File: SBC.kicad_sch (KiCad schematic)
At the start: 0 parts

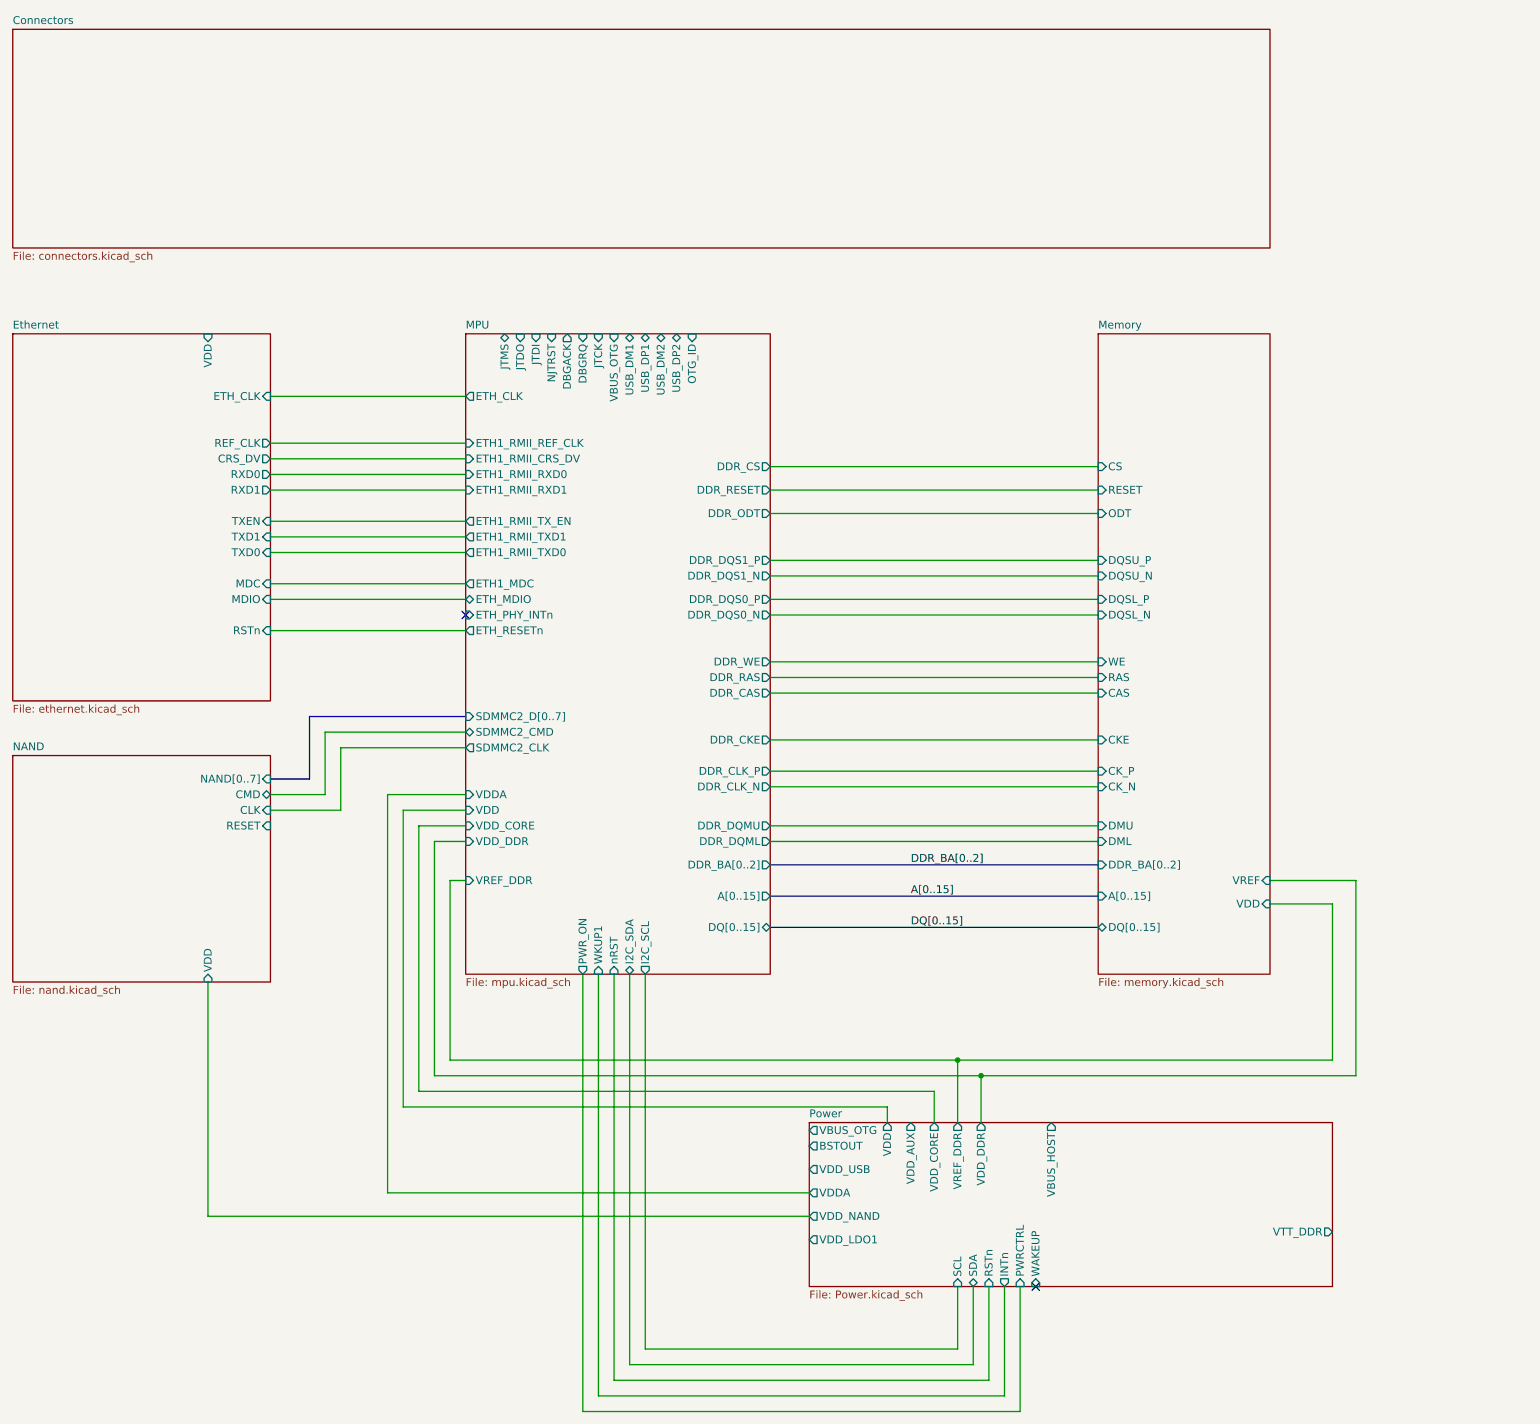
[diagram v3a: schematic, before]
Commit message: Moved connectors to their own sheets
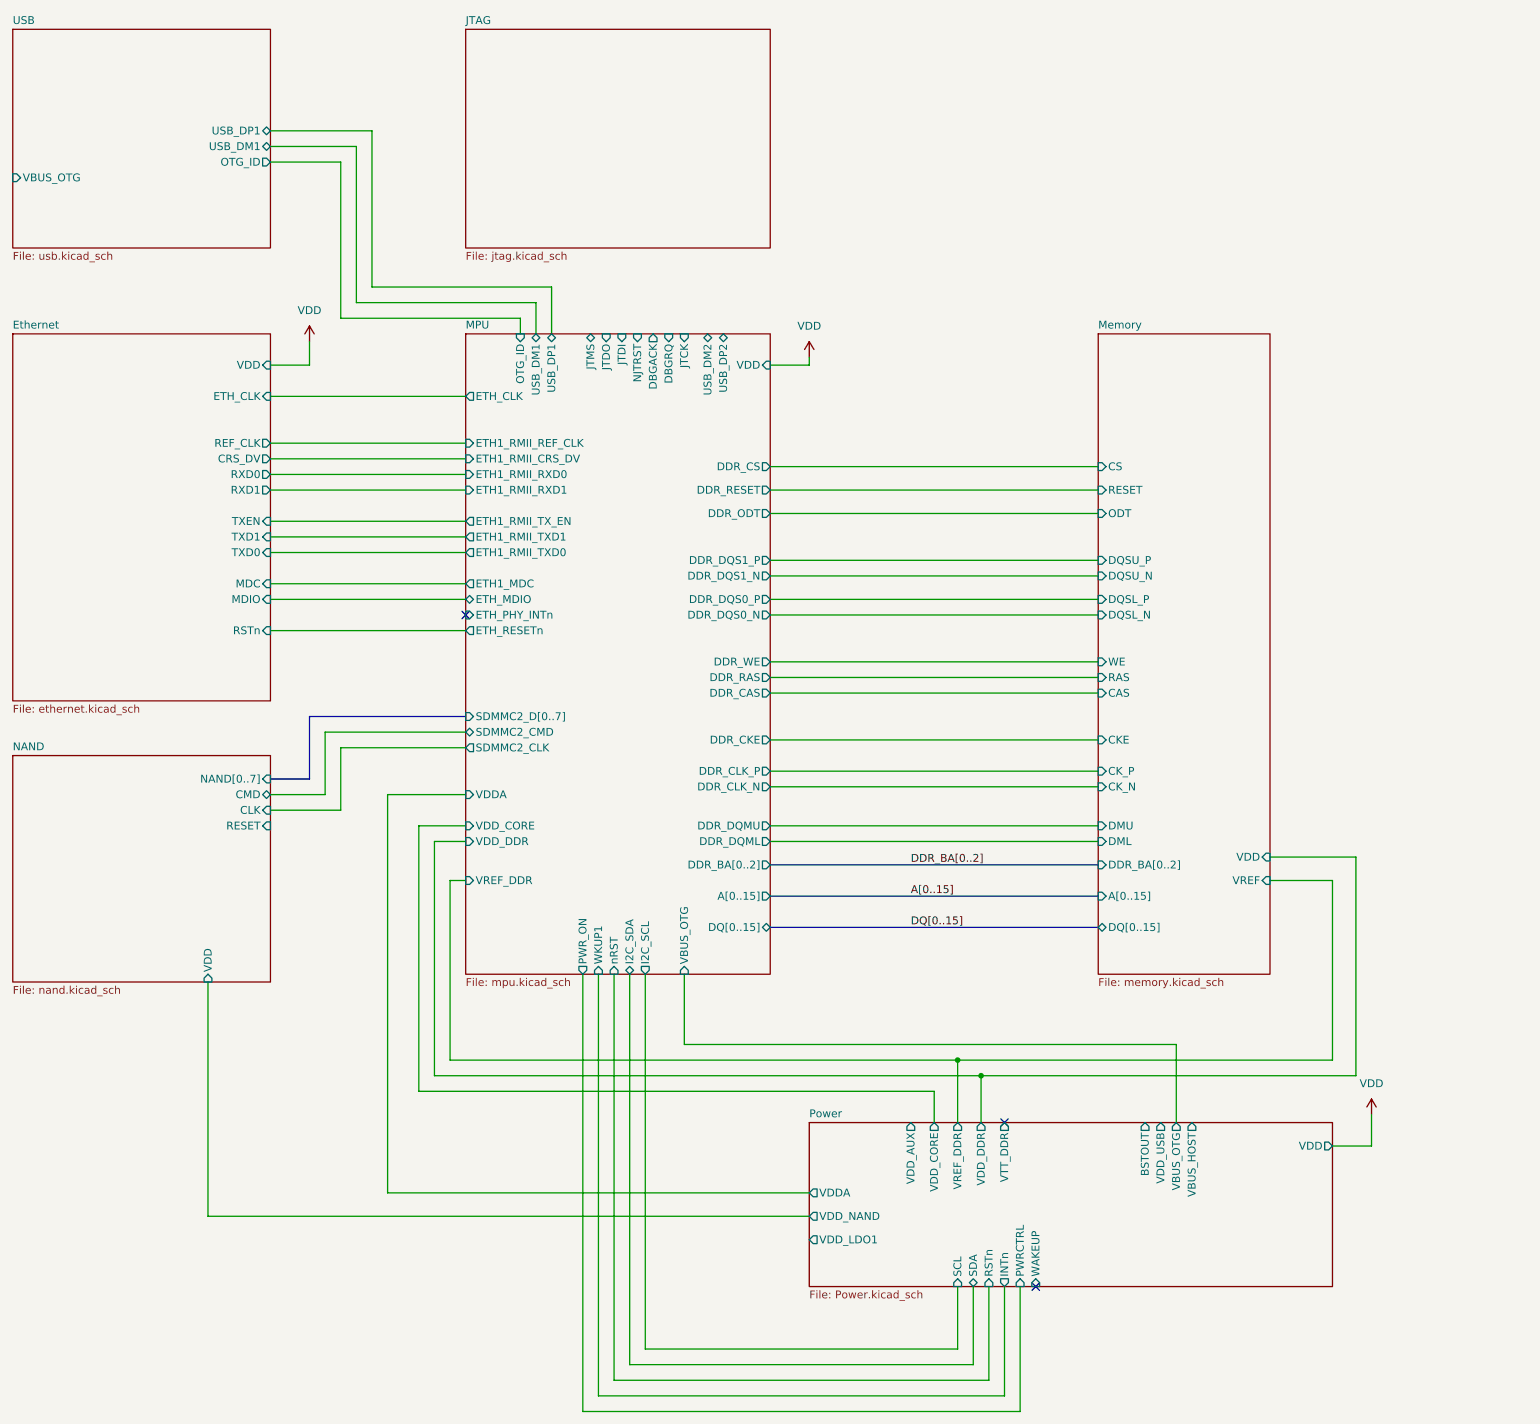
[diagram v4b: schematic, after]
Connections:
- no-connect marks 2 -> 3
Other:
- sheet Connectors renamed JTAG
- added sheet USB (usb.kicad_sch)
- sheet JTAG: file connectors.kicad_sch -> jtag.kicad_sch

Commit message: Finished USB JTAG connectors and cleaned up schematic
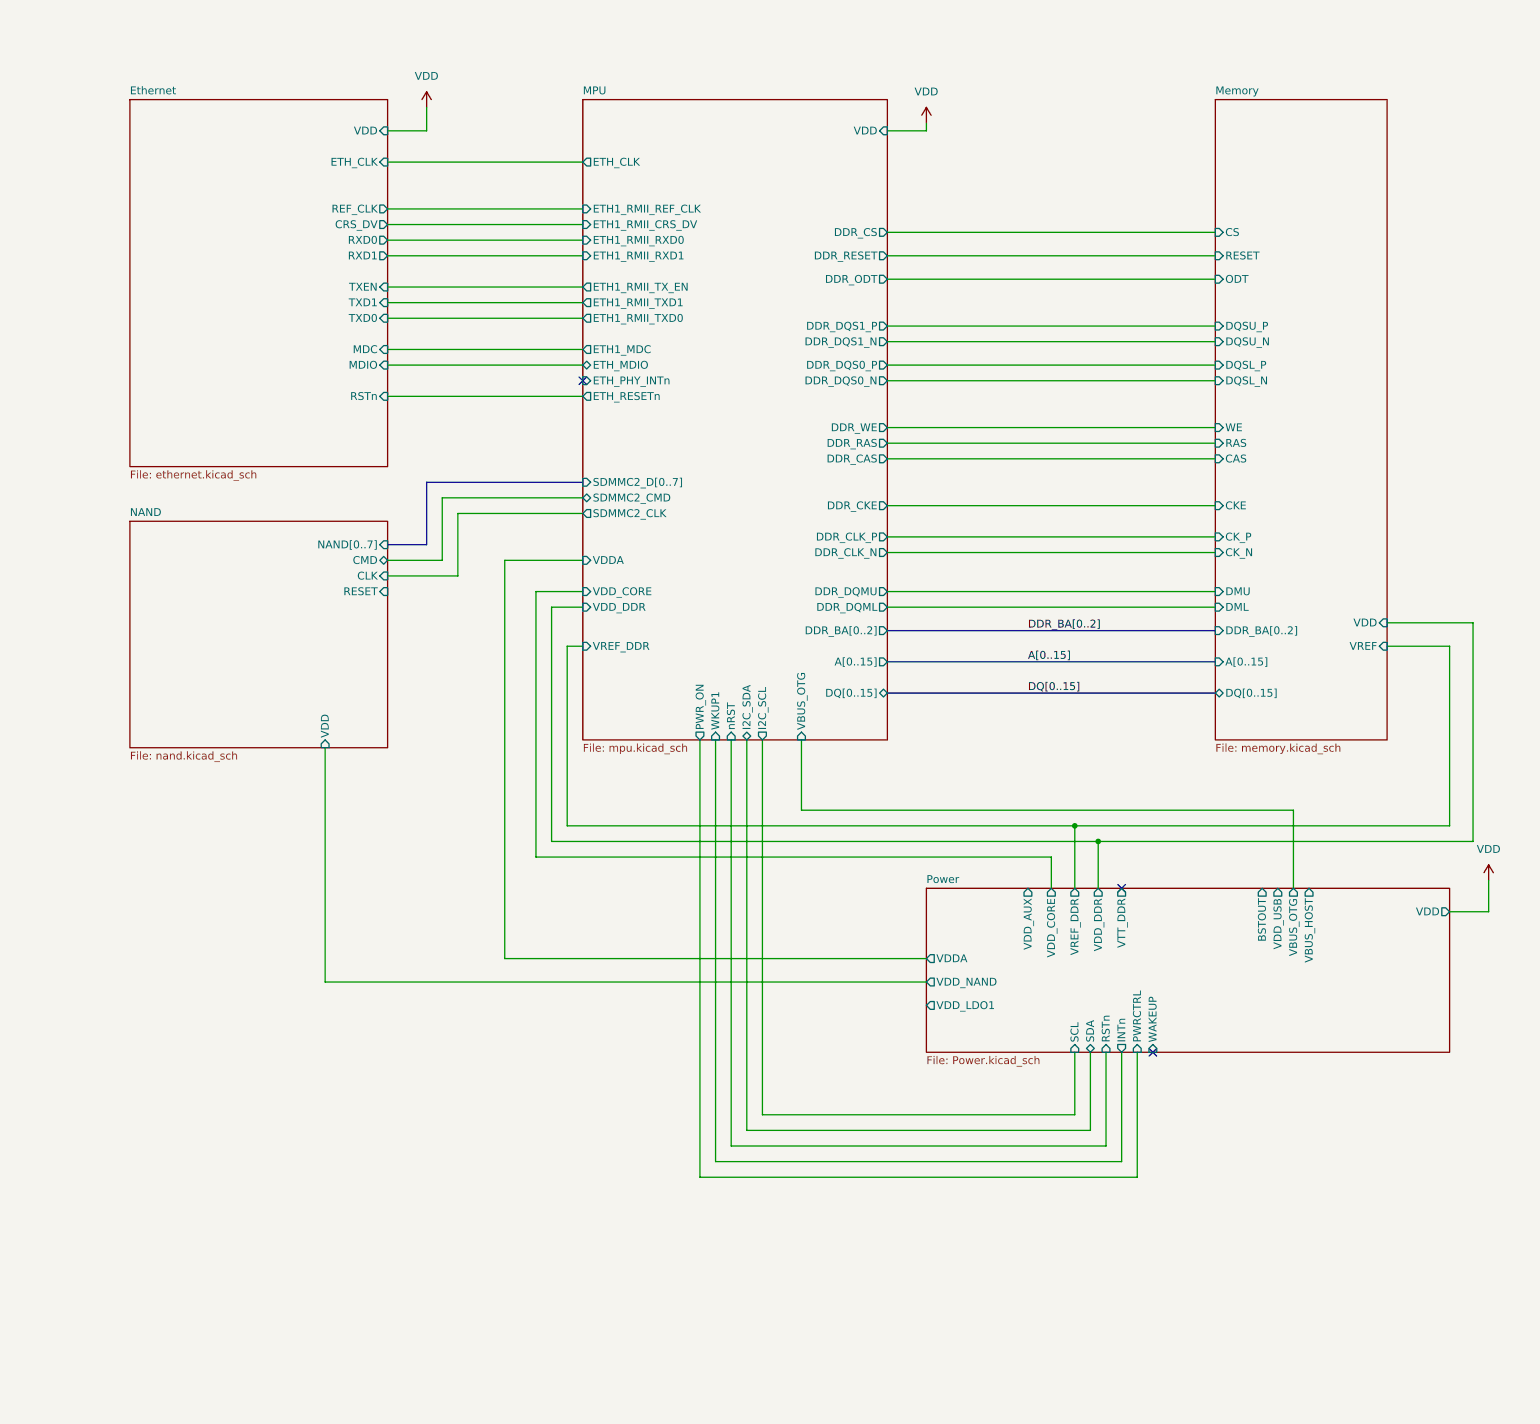
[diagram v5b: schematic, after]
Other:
- removed sheet JTAG
- removed sheet USB
- sheet MPU ports: added none; removed DBGACK, DBGRQ, JTCK, JTDI, JTDO, JTMS, NJTRST, OTG_ID, USB_DM1, USB_DM2, USB_DP1, USB_DP2

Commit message: Adding another usb and cleanup
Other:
- sheet MPU ports: added VBUS_HOST; removed none
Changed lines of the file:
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@@
 	(wire
 		(pts
-			(xy 214.63 153.67) (xy 214.63 142.24)
+			(xy 212.09 153.67) (xy 212.09 142.24)
 		)
 		(stroke
@@
 	(wire
 		(pts
-			(xy 294.64 153.67) (xy 214.63 153.67)
+			(xy 294.64 153.67) (xy 212.09 153.67)
 		)
 		(stroke
@@
 	(wire
 		(pts
+			(xy 297.18 151.13) (xy 214.63 151.13)
+		)
+		(stroke
+			(width 0)
+			(type default)
+		)
+	)
+	(wire
+		(pts
+			(xy 214.63 142.24) (xy 214.63 151.13)
+		)
+		(stroke
+			(width 0)
+			(type default)
+		)
+	)
+	(wire
+		(pts
 			(xy 176.53 127) (xy 179.07 127)
 		)
@@
 		(pts
 			(xy 147.32 86.36) (xy 179.07 86.36)
+		)
+		(stroke
+			(width 0)
+			(type default)
+		)
+	)
+	(wire
+		(pts
+			(xy 297.18 166.37) (xy 297.18 151.13)
 		)
 		(stroke
@@
 		)
 		(pin "VBUS_OTG" input
-			(at 214.63 142.24 270)
+			(at 212.09 142.24 270)
 			(effects
 				(font
@@
 			(effects
 				(font
+					(size 1.27 1.27)
+				)
+				(justify left)
+			)
+		)
+		(pin "VBUS_HOST" output
+			(at 214.63 142.24 270)
+			(effects
+				(font
